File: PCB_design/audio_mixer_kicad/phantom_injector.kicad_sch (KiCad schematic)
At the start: 151 parts, among them U24 MCP23017-E/SO, U25 MIC2981_82YWM-TR, U26 MIC2981_82YWM-TR

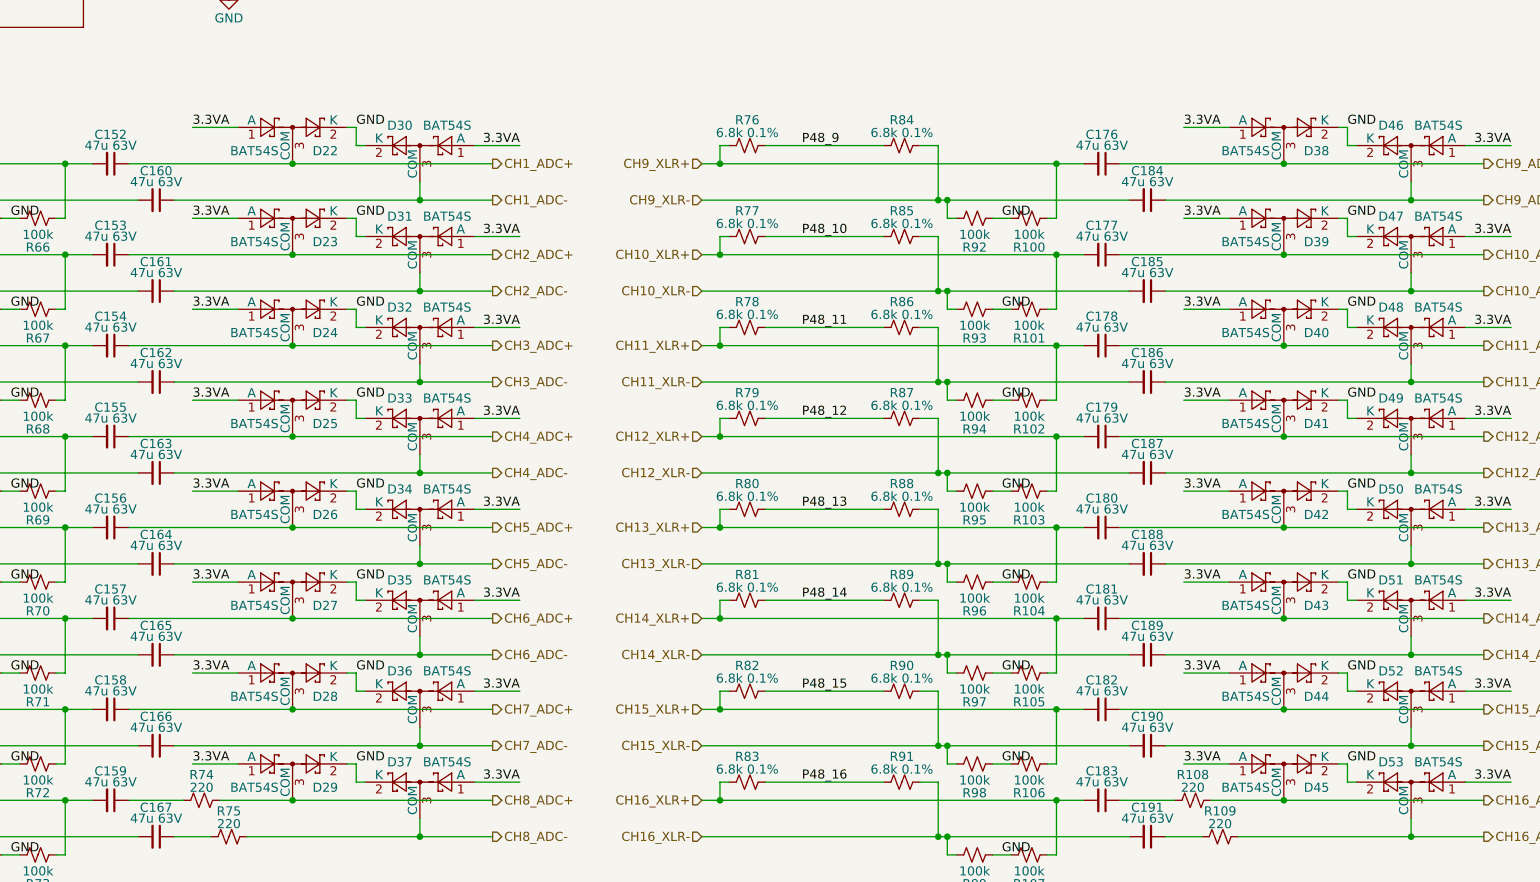
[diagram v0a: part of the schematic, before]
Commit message: Add oscillator and adc input caps
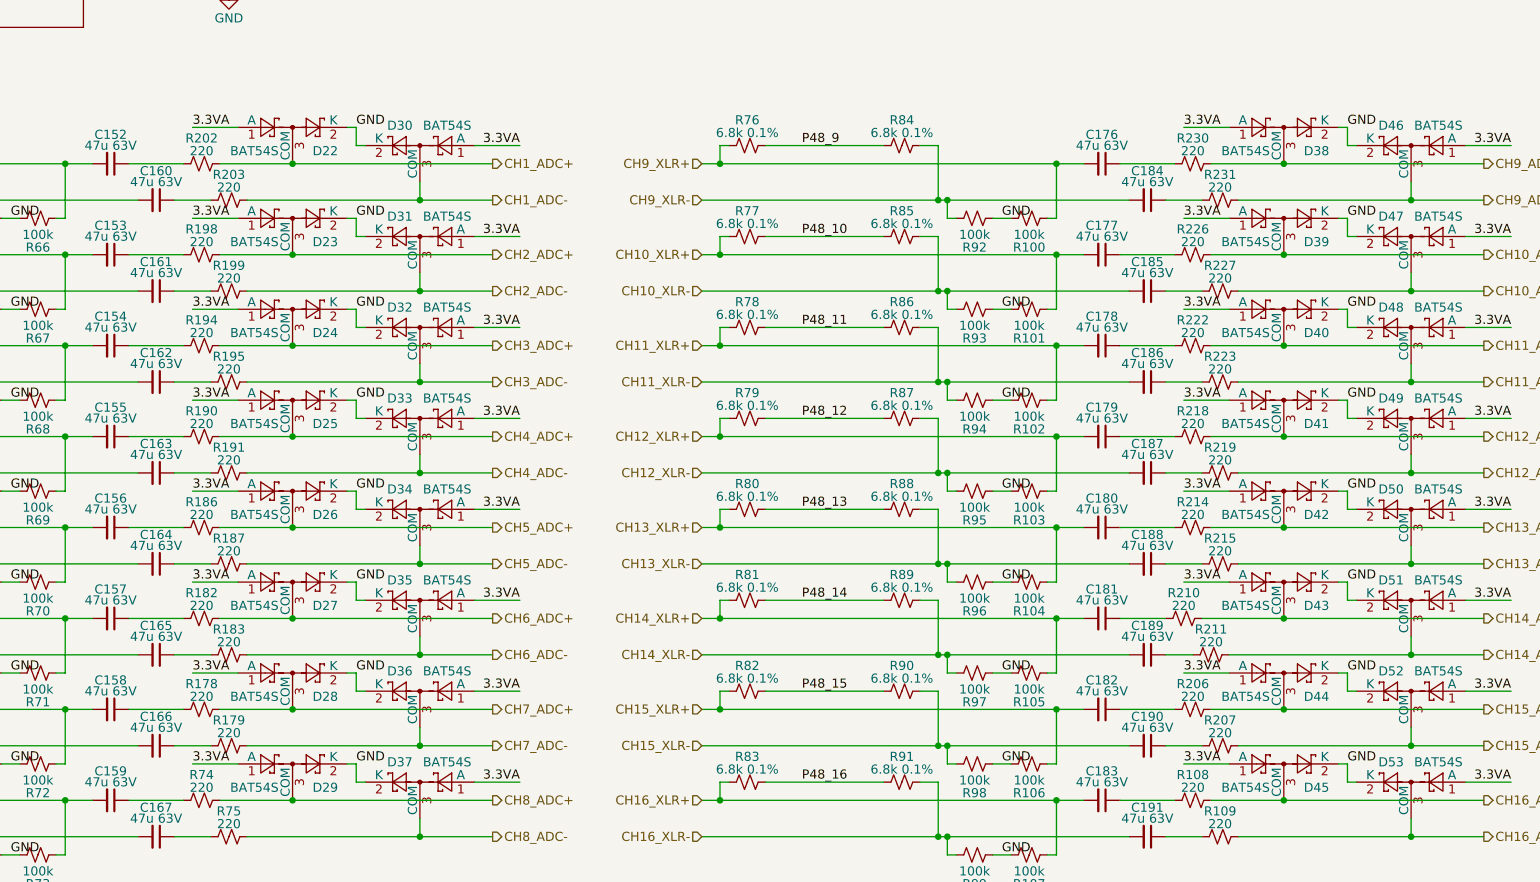
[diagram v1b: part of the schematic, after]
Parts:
- added R178, R179, R182, R183, R186, R187, R190, R191, R194, R195, R198, R199, R202, R203, R206, R207, R210, R211, R214, R215, R218, R219, R222, R223, R226, R227, R230, R231: 220, symbol Device:R_Small_US
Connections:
- net CH10_ADC+: now also R226.2; no longer C177.1
- net CH10_ADC-: now also R227.2; no longer C185.1
- net CH11_ADC+: now also R222.2; no longer C178.1
- net CH11_ADC-: now also R223.2; no longer C186.1
- net CH12_ADC+: now also R218.2; no longer C179.1
- net CH12_ADC-: now also R219.2; no longer C187.1
- net CH13_ADC+: now also R214.2; no longer C180.1
- net CH13_ADC-: now also R215.2; no longer C188.1
- net CH14_ADC+: now also R210.2; no longer C181.1
- net CH14_ADC-: now also R211.2; no longer C189.1
- net CH15_ADC+: now also R206.2; no longer C182.1
- net CH15_ADC-: now also R207.2; no longer C190.1
- net CH1_ADC+: now also R202.2; no longer C152.1
- net CH1_ADC-: now also R203.2; no longer C160.1
- net CH2_ADC+: now also R198.2; no longer C153.1
- net CH2_ADC-: now also R199.2; no longer C161.1
- net CH3_ADC+: now also R194.2; no longer C154.1
- net CH3_ADC-: now also R195.2; no longer C162.1
- net CH4_ADC+: now also R190.2; no longer C155.1
- net CH4_ADC-: now also R191.2; no longer C163.1
- net CH5_ADC+: now also R186.2; no longer C156.1
- net CH5_ADC-: now also R187.2; no longer C164.1
- net CH6_ADC+: now also R182.2; no longer C157.1
- net CH6_ADC-: now also R183.2; no longer C165.1
- net CH7_ADC+: now also R178.2; no longer C158.1
- net CH7_ADC-: now also R179.2; no longer C166.1
- net CH9_ADC+: now also R230.2; no longer C176.1
- net CH9_ADC-: now also R231.2; no longer C184.1
- new net: C179.1, R218.1
- new net: C154.1, R194.1
- new net: C160.1, R203.1
- new net: C155.1, R190.1
- new net: C187.1, R219.1
- new net: C152.1, R202.1
- new net: C165.1, R183.1
- new net: C182.1, R206.1
- new net: C184.1, R231.1
- new net: C156.1, R186.1
- new net: C176.1, R230.1
- new net: C188.1, R215.1
- new net: C157.1, R182.1
- new net: C164.1, R187.1
- new net: C178.1, R222.1
- new net: C158.1, R178.1
- new net: C186.1, R223.1
- new net: C153.1, R198.1
- new net: C180.1, R214.1
- new net: C190.1, R207.1
- new net: C162.1, R195.1
- new net: C177.1, R226.1
- new net: C161.1, R199.1
- new net: C181.1, R210.1
- new net: C166.1, R179.1
- new net: C189.1, R211.1
- new net: C163.1, R191.1
- new net: C185.1, R227.1

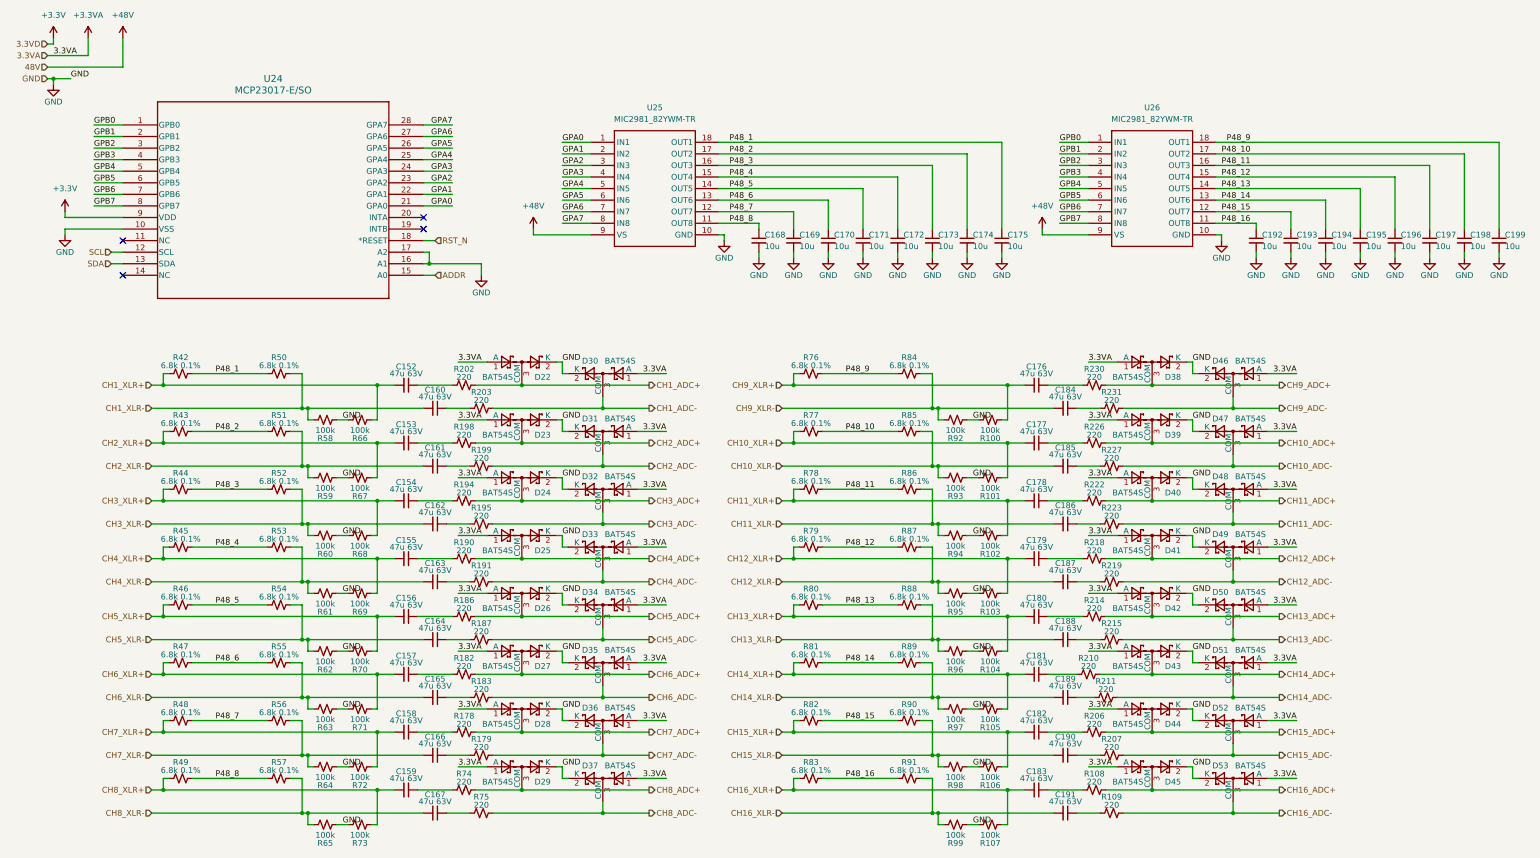
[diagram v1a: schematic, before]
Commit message: Reannotate and add passives for Y1
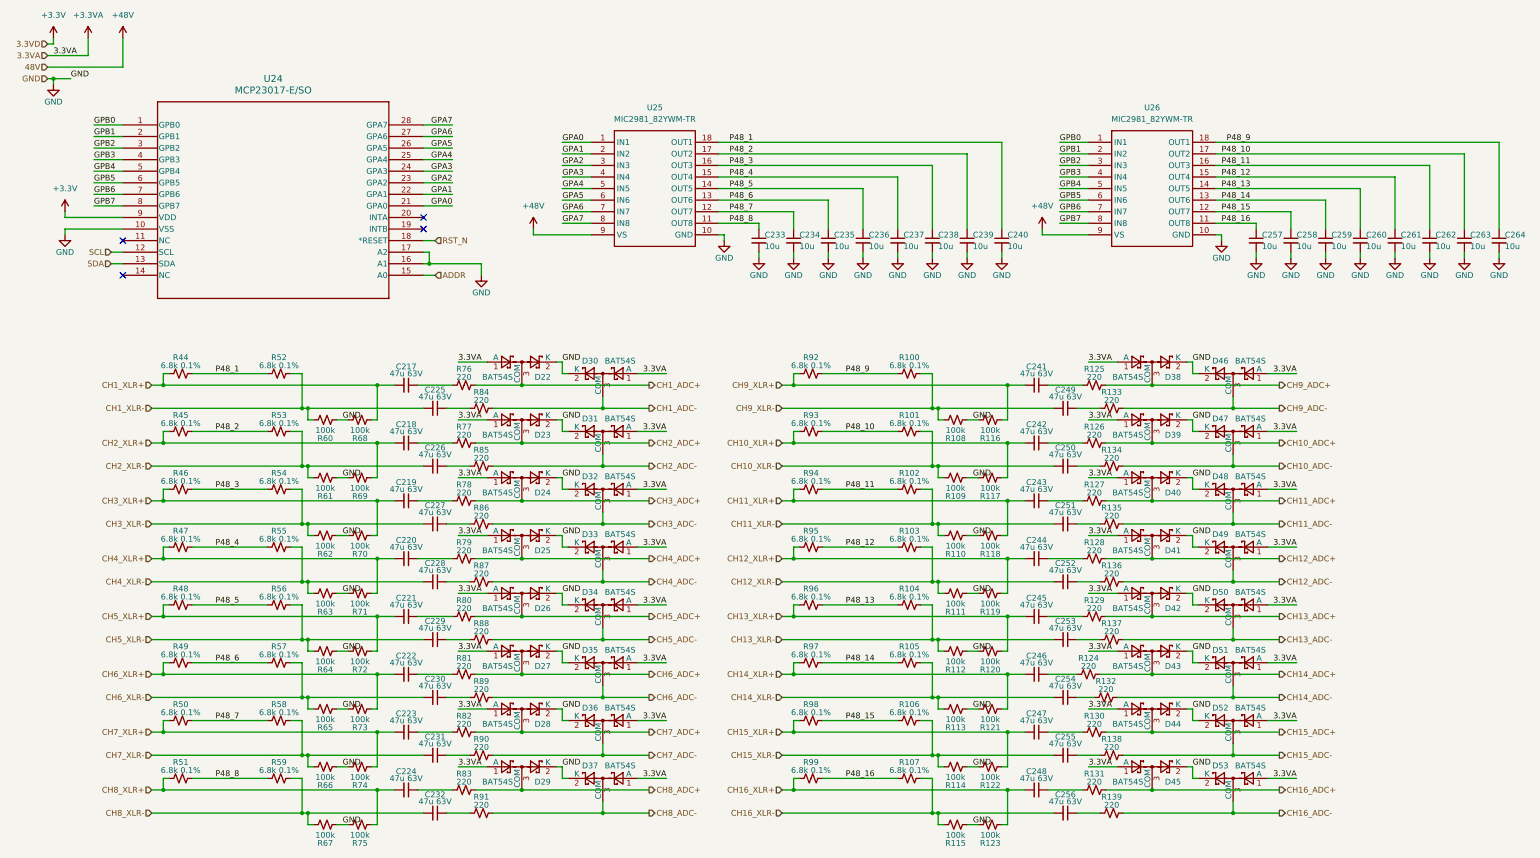
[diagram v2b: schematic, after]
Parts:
- renumbered C152 to C217, C153 to C218, C154 to C219, C155 to C220, C156 to C221, C157 to C222, C158 to C223, C159 to C224, C160 to C225, C161 to C226, C162 to C227, C163 to C228, C164 to C229, C165 to C230, C166 to C231, C167 to C232, C168 to C233, C169 to C234, C170 to C235, C171 to C236, C172 to C237, C173 to C238, C174 to C239, C175 to C240, C176 to C241, C177 to C242, C178 to C243, C179 to C244, C180 to C245, C181 to C246, C182 to C247, C183 to C248, C184 to C249, C185 to C250, C186 to C251, C187 to C252, C188 to C253, C189 to C254, C190 to C255, C191 to C256, C192 to C257, C193 to C258, C194 to C259, C195 to C260, C196 to C261, C197 to C262, C198 to C263, C199 to C264, R84 to R100, R85 to R101, R86 to R102, R87 to R103, R88 to R104, R89 to R105, R90 to R106, R91 to R107, R92 to R108, R93 to R109, R94 to R110, R95 to R111, R96 to R112, R97 to R113, R98 to R114, R99 to R115, R100 to R116, R101 to R117, R102 to R118, R103 to R119, R104 to R120, R105 to R121, R106 to R122, R107 to R123, R210 to R124, R230 to R125, R226 to R126, R222 to R127, R218 to R128, R214 to R129, R206 to R130, R108 to R131, R211 to R132, R231 to R133, R227 to R134, R223 to R135, R219 to R136, R215 to R137, R207 to R138, R109 to R139, R42 to R44, R43 to R45, R44 to R46, R45 to R47, R46 to R48, R47 to R49, R48 to R50, R49 to R51, R50 to R52, R51 to R53, R52 to R54, R53 to R55, R54 to R56, R55 to R57, R56 to R58, R57 to R59, R58 to R60, R59 to R61, R60 to R62, R61 to R63, R62 to R64, R63 to R65, R64 to R66, R65 to R67, R66 to R68, R67 to R69, R68 to R70, R69 to R71, R70 to R72, R71 to R73, R72 to R74, R73 to R75, R202 to R76, R198 to R77, R194 to R78, R190 to R79, R186 to R80, R182 to R81, R178 to R82, R74 to R83, R203 to R84, R199 to R85, R195 to R86, R191 to R87, R187 to R88, R183 to R89, R179 to R90, R75 to R91, R76 to R92, R77 to R93, R78 to R94, R79 to R95, R80 to R96, R81 to R97, R82 to R98, R83 to R99

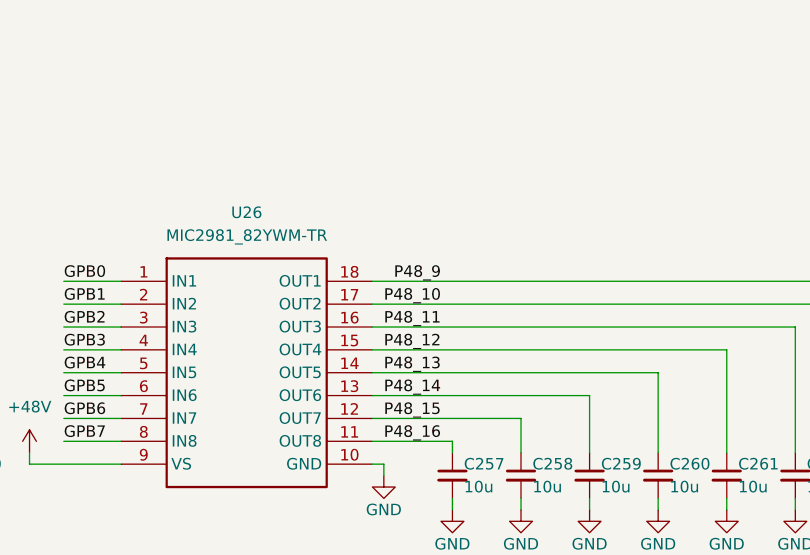
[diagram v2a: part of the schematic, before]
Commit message: Move I2C pins away from FPGA analog ports
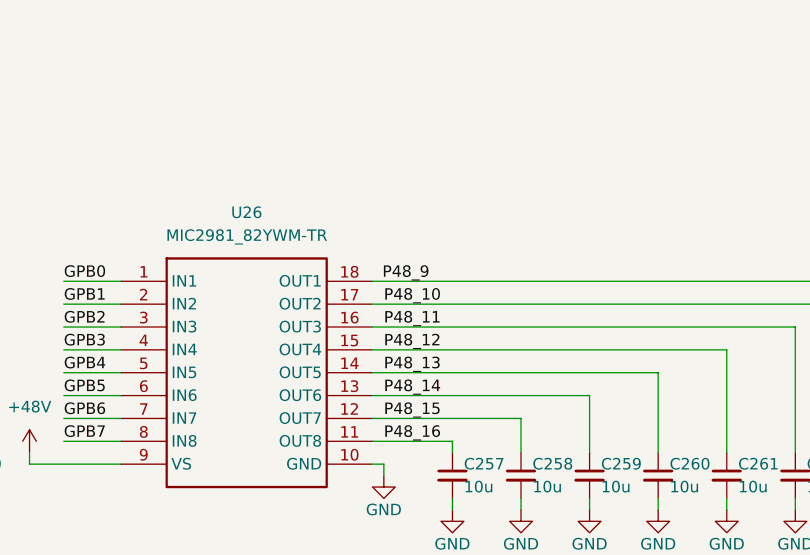
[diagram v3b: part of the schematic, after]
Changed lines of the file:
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@@
 	)
 	(label "P48_9"
-		(at 271.78 30.48 180)
+		(at 270.51 30.48 180)
 		(effects
 			(font
